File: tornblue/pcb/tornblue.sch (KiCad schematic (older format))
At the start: 80 parts, among them J1 BATT, J2 SWD, J3 BREAKOUT, J4 USB C - USB2.0, J5 BATT_PIN, Q1 AO3401A, Q2 AO3401A, SW1 SW_Push, SW10 SW_Push, SW11 SW_Push, SW12 SW_Push, SW13 SW_Push, SW14 SW_Push, SW15 SW_Push, SW16 SW_Push, SW17 SW_Push, SW18 SW_Push, SW19 EC11, SW2 SW_Push, SW20 SW_Push, SW21 SW_Push, SW22 EC11, SW23 RESET, SW24 SW_SPST, SW3 SW_Push, SW4 SW_Push, SW5 SW_Push, SW6 SW_Push, SW7 SW_Push, SW8 SW_Push, SW9 SW_Push, U1 XC6220, U2 TP4056, U3 nRF52840_holyiot_18010, U4 SRV05-4

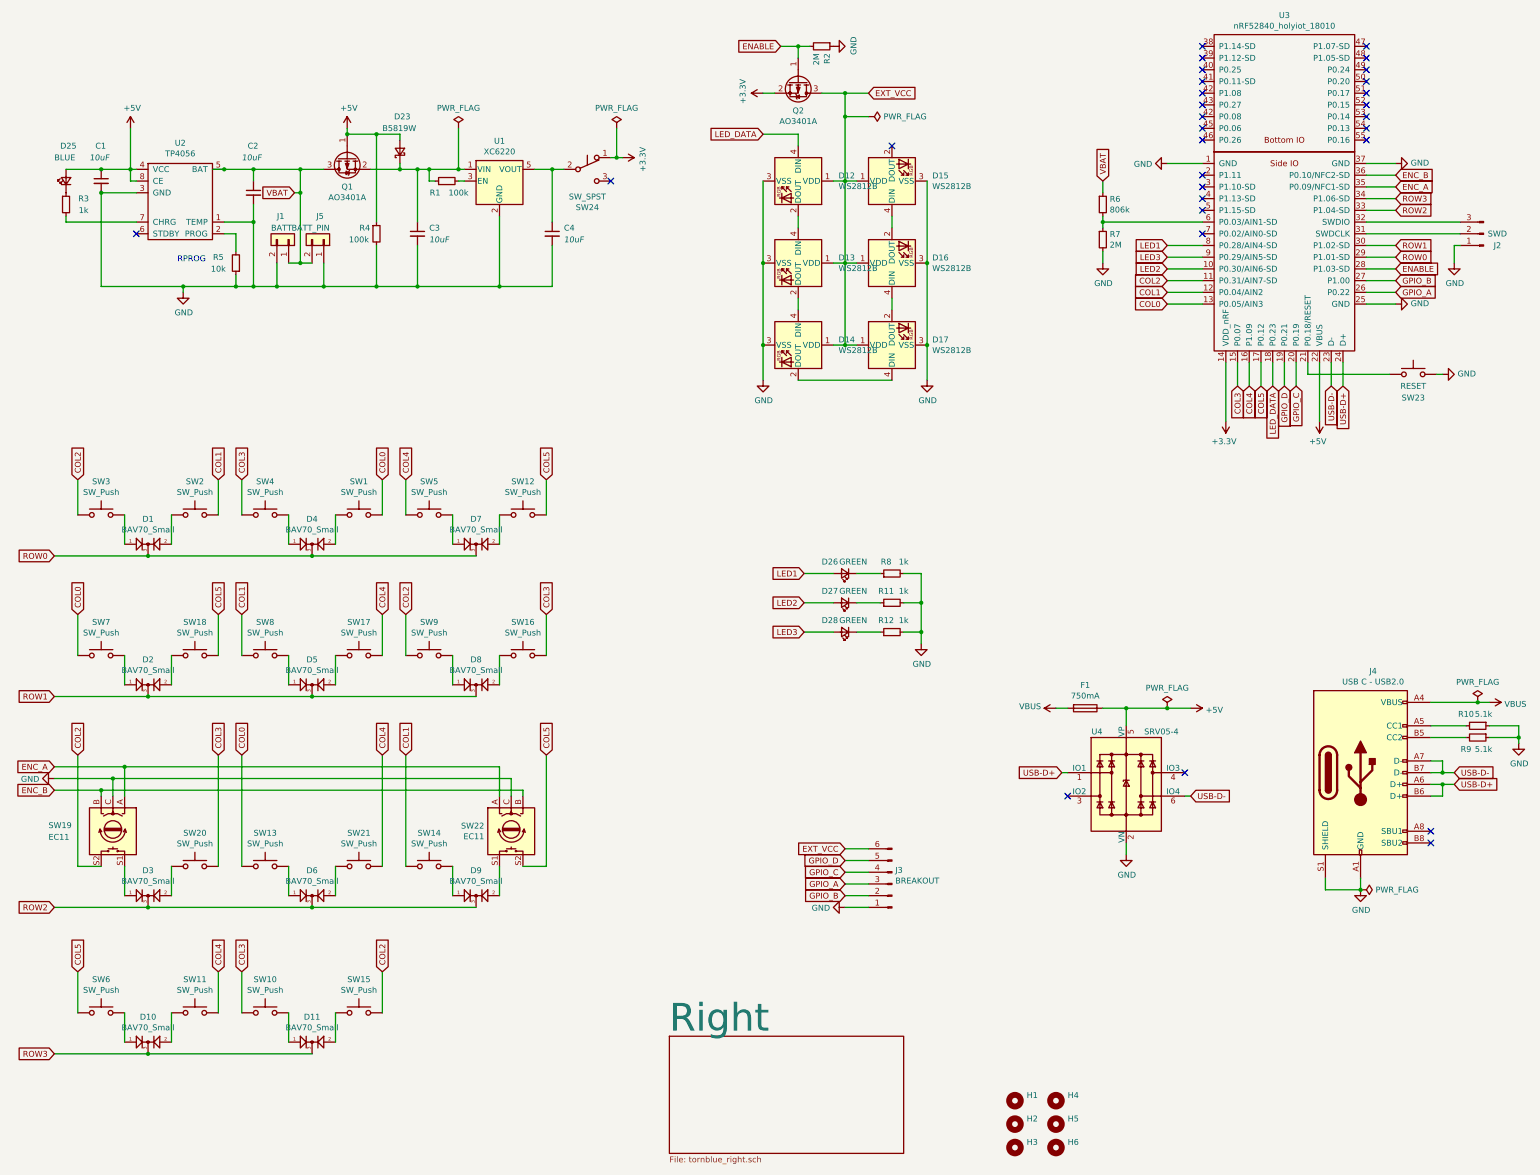
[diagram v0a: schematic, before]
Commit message: Finish layout, via placement and silk screen
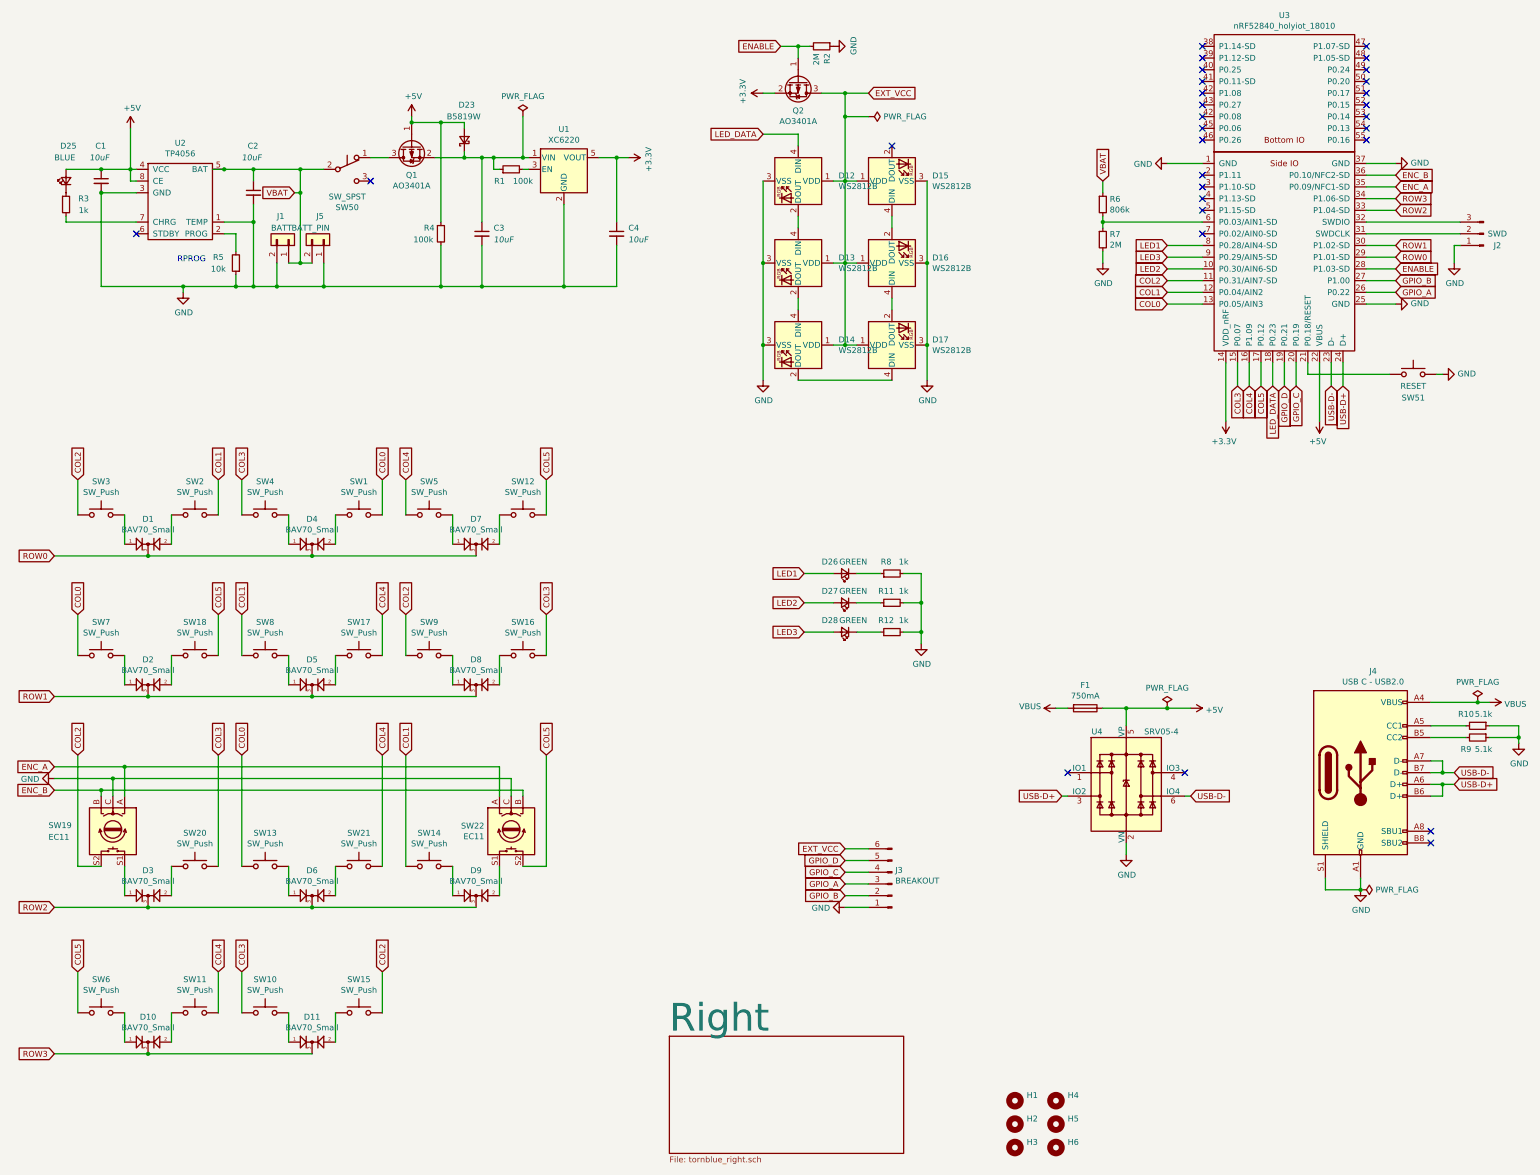
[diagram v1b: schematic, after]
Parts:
- renumbered SW24 to SW50, SW23 to SW51
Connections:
- net +3V3: now also C4.1, U1.5 (VOUT); no longer SW50.1 (A)
- net USB-D+: now also U4.3 (IO2); no longer U4.1 (IO1)
- net VBAT: now also SW50.2 (B); no longer Q1.3 (D)
- new net: Q1.3 (D), SW50.1 (A)
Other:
- moved on the sheet: C3, C4, D23, Q1, R1, R4, SW50, U1

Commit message: Add elecrow files
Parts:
- C1, C2, C3, C4, D1, D10, D11, D2, D23, D25, D26, D27, D28, D3, D4, D5, D6, D7, D8, D9, F1, J4, Q1, Q2, R1, R10, R11, R12, R2, R3, R4, R5, R6, R7, R8, R9, SW51, U1, U2, U4: Mouser (none) -> TODO
- D12, D13, D14, D15, D16, D17: LCSC - -> C2761795; Mouser (none) -> TODO
- H1, H2, H3, H4, H5, H6, J2, J3, SW1, SW10, SW11, SW12, SW13, SW14, SW15, SW16, SW17, SW18, SW19, SW2, SW20, SW21, SW22, SW3, SW4, SW5, SW6, SW7, SW8, SW9: Mouser (none) -> -
- J1: LCSC - -> C295747; Mouser (none) -> TODO
- J5: LCSC (none) -> -; Mouser (none) -> -
- SW50: LCSC (none) -> C221841; Mouser (none) -> TODO
- U3: LCSC - -> nRF52840_holyiot_18010; Mouser (none) -> TODO

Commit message: Update to kicad 6
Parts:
- C1, C2, C3, C4: Mouser TODO -> 187-CL21A106KAYNNNE
- D1, D10, D11, D2, D3, D4, D5, D6, D7, D8, D9: Mouser TODO -> 583-BAV70
- D12, D13, D14, D15, D16, D17: Mouser TODO -> 474-COM-16346
- D23: Mouser TODO -> 833-B5819W-TP
- F1: Mouser TODO -> 504-CC12H750MA-TR
- Q1, Q2: Mouser TODO -> DMP3130L
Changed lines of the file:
@@
 F 3 "https://datasheet.lcsc.com/lcsc/1809211023_Changjiang-Electronics-Tech--CJ-BAV70_C68978.pdf" H 4950 9900 50  0001 C CNN
 F 4 "C68978" H 4950 9900 50  0001 C CNN "LCSC"
-F 5 "TODO" H 4950 9900 50  0001 C CNN "Mouser"
+F 5 "583-BAV70" H 4950 9900 50  0001 C CNN "Mouser"
 	1    4950 9900
 	1    0    0    -1
@@
 F 3 "https://datasheet.lcsc.com/lcsc/1809211023_Changjiang-Electronics-Tech--CJ-BAV70_C68978.pdf" H 3550 8650 50  0001 C CNN
 F 4 "C68978" H 3550 8650 50  0001 C CNN "LCSC"
-F 5 "TODO" H 3550 8650 50  0001 C CNN "Mouser"
+F 5 "583-BAV70" H 3550 8650 50  0001 C CNN "Mouser"
 	1    3550 8650
 	1    0    0    -1
@@
 F 3 "https://datasheet.lcsc.com/lcsc/1809211023_Changjiang-Electronics-Tech--CJ-BAV70_C68978.pdf" H 6350 6850 50  0001 C CNN
 F 4 "C68978" H 6350 6850 50  0001 C CNN "LCSC"
-F 5 "TODO" H 6350 6850 50  0001 C CNN "Mouser"
+F 5 "583-BAV70" H 6350 6850 50  0001 C CNN "Mouser"
 	1    6350 6850
 	1    0    0    -1
@@
 F 3 "https://datasheet.lcsc.com/lcsc/1809211023_Changjiang-Electronics-Tech--CJ-BAV70_C68978.pdf" H 4950 5650 50  0001 C CNN
 F 4 "C68978" H 4950 5650 50  0001 C CNN "LCSC"
-F 5 "TODO" H 4950 5650 50  0001 C CNN "Mouser"
+F 5 "583-BAV70" H 4950 5650 50  0001 C CNN "Mouser"
 	1    4950 5650
 	1    0    0    -1
@@
 F 3 "https://datasheet.lcsc.com/lcsc/1809211023_Changjiang-Electronics-Tech--CJ-BAV70_C68978.pdf" H 6350 5650 50  0001 C CNN
 F 4 "C68978" H 6350 5650 50  0001 C CNN "LCSC"
-F 5 "TODO" H 6350 5650 50  0001 C CNN "Mouser"
+F 5 "583-BAV70" H 6350 5650 50  0001 C CNN "Mouser"
 	1    6350 5650
 	1    0    0    -1
@@
 F 3 "https://datasheet.lcsc.com/lcsc/1809211023_Changjiang-Electronics-Tech--CJ-BAV70_C68978.pdf" H 3550 5650 50  0001 C CNN
 F 4 "C68978" H 3550 5650 50  0001 C CNN "LCSC"
-F 5 "TODO" H 3550 5650 50  0001 C CNN "Mouser"
+F 5 "583-BAV70" H 3550 5650 50  0001 C CNN "Mouser"
 	1    3550 5650
 	1    0    0    -1
@@
 F 3 "https://datasheet.lcsc.com/lcsc/1809211023_Changjiang-Electronics-Tech--CJ-BAV70_C68978.pdf" H 3550 9900 50  0001 C CNN
 F 4 "C68978" H 3550 9900 50  0001 C CNN "LCSC"
-F 5 "TODO" H 3550 9900 50  0001 C CNN "Mouser"
+F 5 "583-BAV70" H 3550 9900 50  0001 C CNN "Mouser"
 	1    3550 9900
 	1    0    0    -1
@@
 F 3 "https://datasheet.lcsc.com/lcsc/1809211023_Changjiang-Electronics-Tech--CJ-BAV70_C68978.pdf" H 3550 6850 50  0001 C CNN
 F 4 "C68978" H 3550 6850 50  0001 C CNN "LCSC"
-F 5 "TODO" H 3550 6850 50  0001 C CNN "Mouser"
+F 5 "583-BAV70" H 3550 6850 50  0001 C CNN "Mouser"
 	1    3550 6850
 	1    0    0    -1
@@
 F 3 "https://cdn-shop.adafruit.com/datasheets/WS2812B.pdf" H 10000 2175 50  0001 L TNN
 F 4 "C2761795" H 9900 2550 50  0001 C CNN "LCSC"
-F 5 "TODO" H 9900 2550 50  0001 C CNN "Mouser"
+F 5 "474-COM-16346" H 9900 2550 50  0001 C CNN "Mouser"
 	1    9900 2550
 	0    -1   -1   0
@@
 F 3 "https://cdn-shop.adafruit.com/datasheets/WS2812B.pdf" H 10000 2875 50  0001 L TNN
 F 4 "C2761795" H 9900 3250 50  0001 C CNN "LCSC"
-F 5 "TODO" H 9900 3250 50  0001 C CNN "Mouser"
+F 5 "474-COM-16346" H 9900 3250 50  0001 C CNN "Mouser"
 	1    9900 3250
 	0    -1   -1   0
@@
 F 3 "https://cdn-shop.adafruit.com/datasheets/WS2812B.pdf" H 10000 3575 50  0001 L TNN
 F 4 "C2761795" H 9900 3950 50  0001 C CNN "LCSC"
-F 5 "TODO" H 9900 3950 50  0001 C CNN "Mouser"
+F 5 "474-COM-16346" H 9900 3950 50  0001 C CNN "Mouser"
 	1    9900 3950
 	0    -1   -1   0
@@
 F 3 "https://cdn-shop.adafruit.com/datasheets/WS2812B.pdf" H 9200 3575 50  0001 L TNN
 F 4 "C2761795" H 9100 3950 50  0001 C CNN "LCSC"
-F 5 "TODO" H 9100 3950 50  0001 C CNN "Mouser"
+F 5 "474-COM-16346" H 9100 3950 50  0001 C CNN "Mouser"
 	1    9100 3950
 	0    1    1    0
@@
 F 3 "https://cdn-shop.adafruit.com/datasheets/WS2812B.pdf" H 9200 2875 50  0001 L TNN
 F 4 "C2761795" H 9100 3250 50  0001 C CNN "LCSC"
-F 5 "TODO" H 9100 3250 50  0001 C CNN "Mouser"
+F 5 "474-COM-16346" H 9100 3250 50  0001 C CNN "Mouser"
 	1    9100 3250
 	0    1    1    0
@@
 F 3 "https://cdn-shop.adafruit.com/datasheets/WS2812B.pdf" H 9200 2175 50  0001 L TNN
 F 4 "C2761795" H 9100 2550 50  0001 C CNN "LCSC"
-F 5 "TODO" H 9100 2550 50  0001 C CNN "Mouser"
+F 5 "474-COM-16346" H 9100 2550 50  0001 C CNN "Mouser"
 	1    9100 2550
 	0    1    1    0
@@
 F 3 "https://datasheet.lcsc.com/lcsc/1809211023_Changjiang-Electronics-Tech--CJ-BAV70_C68978.pdf" H 6350 8650 50  0001 C CNN
 F 4 "C68978" H 6350 8650 50  0001 C CNN "LCSC"
-F 5 "TODO" H 6350 8650 50  0001 C CNN "Mouser"
+F 5 "583-BAV70" H 6350 8650 50  0001 C CNN "Mouser"
 	1    6350 8650
 	1    0    0    -1
@@
 F 3 "http://www.aosmd.com/pdfs/datasheet/AO3401A.pdf" H 9100 1700 50  0001 L CNN
 F 4 "C15127" H 9100 1700 50  0001 C CNN "LCSC"
-F 5 "TODO" H 9100 1700 50  0001 C CNN "Mouser"
+F 5 "DMP3130L" H 9100 1700 50  0001 C CNN "Mouser"
 	1    9100 1700
 	0    1    1    0
@@
 F 3 "https://datasheet.lcsc.com/lcsc/1809211023_Changjiang-Electronics-Tech--CJ-BAV70_C68978.pdf" H 4950 8650 50  0001 C CNN
 F 4 "C68978" H 4950 8650 50  0001 C CNN "LCSC"
-F 5 "TODO" H 4950 8650 50  0001 C CNN "Mouser"
+F 5 "583-BAV70" H 4950 8650 50  0001 C CNN "Mouser"
 	1    4950 8650
 	1    0    0    -1
@@
 F 3 "https://datasheet.lcsc.com/lcsc/1809211023_Changjiang-Electronics-Tech--CJ-BAV70_C68978.pdf" H 4950 6850 50  0001 C CNN
 F 4 "C68978" H 4950 6850 50  0001 C CNN "LCSC"
-F 5 "TODO" H 4950 6850 50  0001 C CNN "Mouser"
+F 5 "583-BAV70" H 4950 6850 50  0001 C CNN "Mouser"
 	1    4950 6850
 	1    0    0    -1
@@
 F 3 "https://datasheet.lcsc.com/lcsc/1811121310_Samsung-Electro-Mechanics-CL21A106KAYNNNE_C15850.pdf" H 3150 2550 50  0001 C CNN
 F 4 "C15850" H 3150 2550 50  0001 C CNN "LCSC"
-F 5 "TODO" H 3150 2550 50  0001 C CNN "Mouser"
+F 5 "187-CL21A106KAYNNNE" H 3150 2550 50  0001 C CNN "Mouser"
 	1    3150 2550
 	1    0    0    -1
@@
 F 3 "https://datasheet.lcsc.com/lcsc/1811121310_Samsung-Electro-Mechanics-CL21A106KAYNNNE_C15850.pdf" H 4450 2650 50  0001 C CNN
 F 4 "C15850" H 4450 2650 50  0001 C CNN "LCSC"
-F 5 "TODO" H 4450 2650 50  0001 C CNN "Mouser"
+F 5 "187-CL21A106KAYNNNE" H 4450 2650 50  0001 C CNN "Mouser"
 	1    4450 2650
 	1    0    0    -1
@@
 F 3 "http://www.aosmd.com/pdfs/datasheet/AO3401A.pdf" H 5800 2250 50  0001 L CNN
 F 4 "C15127" H 5800 2250 50  0001 C CNN "LCSC"
-F 5 "TODO" H 5800 2250 50  0001 C CNN "Mouser"
+F 5 "DMP3130L" H 5800 2250 50  0001 C CNN "Mouser"
 	1    5800 2250
 	0    -1   1    0
@@
 F 3 "https://datasheet.lcsc.com/lcsc/1811121310_Samsung-Electro-Mechanics-CL21A106KAYNNNE_C15850.pdf" H 7550 3000 50  0001 C CNN
 F 4 "C15850" H 7550 3000 50  0001 C CNN "LCSC"
-F 5 "TODO" H 7550 3000 50  0001 C CNN "Mouser"
+F 5 "187-CL21A106KAYNNNE" H 7550 3000 50  0001 C CNN "Mouser"
 	1    7550 3000
 	1    0    0    -1
@@
 F 3 "https://datasheet.lcsc.com/lcsc/1811121310_Samsung-Electro-Mechanics-CL21A106KAYNNNE_C15850.pdf" H 6400 3000 50  0001 C CNN
 F 4 "C15850" H 6400 3000 50  0001 C CNN "LCSC"
-F 5 "TODO" H 6400 3000 50  0001 C CNN "Mouser"
+F 5 "187-CL21A106KAYNNNE" H 6400 3000 50  0001 C CNN "Mouser"
 	1    6400 3000
 	1    0    0    -1
@@
 F 3 "https://datasheet.lcsc.com/lcsc/1809140216_Changjiang-Electronics-Tech--CJ-B5819W-SL_C8598.pdf" V 6250 2200 50  0001 C CNN
 F 4 "C8598" H 6250 2200 50  0001 C CNN "LCSC"
-F 5 "TODO" H 6250 2200 50  0001 C CNN "Mouser"
+F 5 "833-B5819W-TP" H 6250 2200 50  0001 C CNN "Mouser"
 	1    6250 2200
 	0    -1   -1   0
@@
 F 3 "https://datasheet.lcsc.com/lcsc/1912111437_BUSSMANN-CC12H750MA-TR_C328915.pdf~" H 11550 7050 50  0001 C CNN
 F 4 "C328915" H 11550 7050 50  0001 C CNN "LCSC"
-F 5 "TODO" H 11550 7050 50  0001 C CNN "Mouser"
+F 5 "504-CC12H750MA-TR" H 11550 7050 50  0001 C CNN "Mouser"
 	1    11550 7050
 	0    1    1    0
